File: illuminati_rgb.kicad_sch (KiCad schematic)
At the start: 47 parts, among them IC1 TPS564247DRLR, IC2 SPH0645LM4H-1-8, J1 Conn_02x03_Odd_Even, J2 Conn_01x04, J3 Conn_01x02, J6 Conn_01x02, J7 Conn_01x04, J8 Conn_01x04, Q1 C351406, Q2 C351406, Q3 C351406, Q4 C351406, Q5 C351406, Q6 C351406, Q7 C351406, Q8 C351406, Q9 C351406, SW1 SW_SPST, U1 ESP32-WROOM-32

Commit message: v2 board
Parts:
- removed C5: 22u, Capacitor_SMD:C_0805_2012Metric, symbol Device:C
- removed IC1: TPS564247DRLR, SamacSys_Parts:SOT50P160X60-6N, symbol SamacSys_Parts:TPS564247DRLR
- removed IC2: SPH0645LM4H-1-8, SamacSys_Parts:SPH0645LM4H18, symbol SamacSys_Parts:SPH0645LM4H-1-8
- removed J2, J7, J8: Conn_01x04, TerminalBlock_Phoenix:TerminalBlock_Phoenix_MKDS-1,5-4_1x04_P5.00mm_Horizontal, symbol Connector_Generic:Conn_01x04
- removed J3, J6: Conn_01x02, TerminalBlock_Phoenix:TerminalBlock_Phoenix_MKDS-1,5-2_1x02_P5.00mm_Horizontal, symbol Connector_Generic:Conn_01x02
- removed Q1, Q2, Q3, Q4, Q5, Q6, Q7, Q8, Q9: C351406, Package_TO_SOT_SMD:SOT-23, symbol Device:Q_NMOS_GSD
- removed R10, R6, R9: 10k, Resistor_SMD:R_0805_2012Metric, symbol Device:R
- removed R11: 100k, Resistor_SMD:R_0603_1608Metric_Pad0.98x0.95mm_HandSolder, symbol Device:R
- removed R12: 22k, Resistor_SMD:R_0603_1608Metric_Pad0.98x0.95mm_HandSolder, symbol Device:R
- removed R13: NC, Resistor_SMD:R_0805_2012Metric, symbol Device:R
- removed R14: 0R, Resistor_SMD:R_0805_2012Metric, symbol Device:R
- removed R15: 10k, Resistor_SMD:R_0402_1005Metric, symbol Device:R
- removed R16: 20k, Resistor_SMD:R_0402_1005Metric, symbol Device:R
- removed SW1: SW_SPST, Button_Switch_THT:SW_PUSH_6mm_H5mm, symbol Switch:SW_SPST
- removed U1: ESP32-WROOM-32, RF_Module:ESP32-WROOM-32, symbol RF_Module:ESP32-WROOM-32
- added C1: 10u/1206, Capacitor_SMD:C_1206_3216Metric, symbol Device:C
- added C11, C12, C13, C8: 22u, Capacitor_SMD:C_0805_2012Metric, symbol Device:C
- added D1: B340A, Diode_SMD:D_SMA, symbol Device:D_Schottky
- added IC1: ESP32-C3-WROOM-02-N4, SamacSys_Parts:ESP32C3WROOM02N4, symbol SamacSys_Parts:ESP32-C3-WROOM-02-N4
- added J1: Conn_01x04, TerminalBlock_Phoenix:TerminalBlock_Phoenix_MKDS-1,5-4_1x04_P5.00mm_Horizontal, symbol Connector_Generic:Conn_01x04
- added JP1, JP2, JP3, JP4, JP5: Jumper_2_Bridged, Jumper:SolderJumper-2_P1.3mm_Bridged_RoundedPad1.0x1.5mm, symbol Jumper:Jumper_2_Bridged
- added PS1: AP5100WG-7, SamacSys_Parts:SOT95P285X140-6N, symbol SamacSys_Parts:AP5100WG-7
- added R1: 10k, Resistor_SMD:R_0603_1608Metric, symbol Device:R
- added U1: AMS1117-3.3, Package_TO_SOT_SMD:SOT-223-3_TabPin2, symbol Regulator_Linear:AMS1117-3.3
- added U2, U3, U4: 74HC14, Package_SO:SOIC-14_3.9x8.7mm_P1.27mm, symbol 74xx:74HC14
- C10: renamed from C8; value 10u -> 22u; footprint Capacitor_SMD:C_0805_2012Metric_Pad1.18x1.45mm_HandSolder -> Capacitor_SMD:C_0805_2012Metric
- C2: value 22u -> 10u/1206; footprint Capacitor_SMD:C_0805_2012Metric -> Capacitor_SMD:C_1206_3216Metric
- C3: value 100n -> 22n; footprint Capacitor_SMD:C_0603_1608Metric_Pad1.08x0.95mm_HandSolder -> Capacitor_SMD:C_0603_1608Metric
- C4, C9: value 100n -> 22u; footprint Capacitor_SMD:C_0603_1608Metric_Pad1.08x0.95mm_HandSolder -> Capacitor_SMD:C_0805_2012Metric
- C5: renamed from C1; footprint Capacitor_SMD:C_0805_2012Metric_Pad1.18x1.45mm_HandSolder -> Capacitor_SMD:C_0603_1608Metric
- C7: value 56p -> 100p; footprint Capacitor_SMD:C_0603_1608Metric_Pad1.08x0.95mm_HandSolder -> Capacitor_SMD:C_0603_1608Metric
- L1: value 1.5u -> 10u/C2921170; footprint Inductor_SMD:L_Wuerth_MAPI-4020 -> Inductor_SMD:L_Chilisin_BMRA00040420
- R2, R3, R4, R7: footprint Resistor_SMD:R_0805_2012Metric -> Resistor_SMD:R_0603_1608Metric
- R5, R8: value 10k -> 2k; footprint Resistor_SMD:R_0805_2012Metric -> Resistor_SMD:R_0603_1608Metric
- R6: renamed from R1; footprint Resistor_SMD:R_0805_2012Metric -> Resistor_SMD:R_0603_1608Metric
- renumbered J1 to J2
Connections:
- net +3V3: now also C9.1, R2.1, R3.1, IC1.1 (3V3), R1.1, U1.2 (VO); no longer C4.1, C6.1, C7.1, C9.2, L1.1
- net B1: now also IC1.5 (IO6), U2.5; no longer R8.1
- net B2: now also JP3.2 (B), U2.13
- net B3: now also IC1.13 (IO18), U3.1
- net G1: now also IC1.4 (IO5), U2.3; no longer R5.1
- net G2: now also JP5.2 (B), U2.11
- net G3: now also IC1.14 (IO19), U3.3; no longer R7.1
- net GND: now also C9.2, R5.1, C1.2, C11.2, C12.2, C13.2, C8.2, D1.2 (A), IC1.19 (GND_2), IC1.20 (GND_3), IC1.21 (GND_4), IC1.22 (GND_5), IC1.23 (GND_6), IC1.24 (GND_7), IC1.25 (GND_8), IC1.26 (GND_9), IC1.27 (GND_10), IC1.9 (GND_1), J1.3 (Pin_3), J1.4 (Pin_4), PS1.2 (GND), U1.1 (GND), U2.7 (GND), U3.7 (GND), U4.7 (GND); no longer C3.2, C9.1, R2.2, R3.2, R4.2, R5.2, R7.2
- net R1: now also IC1.3 (IO4), U2.1; no longer R2.1
- net R2: now also IC1.6 (IO7), U2.9; no longer R3.1
- net R3: now also IC1.15 (IO3), U3.5; no longer R4.1
- net VCC: now also R4.2, C1.1, J1.1 (Pin_1), J1.2 (Pin_2), PS1.5 (IN); no longer C3.1
- net boot: now also R3.2, IC1.8 (IO9), JP3.1 (A)
- net esp_en: now also IC1.2 (EN)
- net rx: now also IC1.11 (RXD), JP1.1 (A)
- net tx: now also IC1.12 (TXD), JP2.1 (A)
- net +5V: now reaches L1.2
- net +5V: now also C4.1, C6.1, C7.1, R7.1, C11.1, C12.1, C13.1, C8.1, U1.3 (VI), U2.14 (VCC), U3.14 (VCC), U4.14 (VCC)
- net V_FB: now reaches C7.2
- net V_FB: now also R7.2, R8.1, PS1.3 (FB)
- new net: C3.2, D1.1 (K), L1.1, PS1.6 (SW)
- new net: PS1.4 (EN), R4.1, R5.2
- new net: C3.1, PS1.1 (BST)
- new net B4: IC1.10 (IO10), U3.13
- new net B5: IC1.18 (IO0), U4.5
- new net G4: JP1.2 (B), U3.11
- new net G5: IC1.17 (IO1), U4.3
- new net R4: JP2.2 (B), U3.9
- new net R5: JP4.2 (B), U4.1
- new net RGB Channel1/B: U2.6
- new net RGB Channel1/G: U2.4
- new net RGB Channel1/R: U2.2
- new net RGB Channel2/B: U2.12
- new net RGB Channel2/G: U2.10
- new net RGB Channel2/R: U2.8
- new net RGB Channel3/B: U3.2
- new net RGB Channel3/G: U3.4
- new net RGB Channel3/R: U3.6
- new net RGB Channel4/B: U3.12
- new net RGB Channel4/G: U3.10
- new net RGB Channel4/R: U3.8
- new net RGB Channel5/B: U4.6
- new net RGB Channel5/G: U4.4
- new net RGB Channel5/R: U4.2
- new net gpio2: IC1.16 (IO2), JP4.1 (A), R2.2
- new net gpio8: IC1.7 (IO8), JP5.1 (A), R1.2
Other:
- added sheet RGB Channel1 (rgb.kicad_sch)
- added sheet RGB Channel2 (rgb.kicad_sch)
- added sheet RGB Channel3 (rgb.kicad_sch)
- added sheet RGB Channel4 (rgb.kicad_sch)
- added sheet RGB Channel5 (rgb.kicad_sch)
- note added: "R19 = (10k * 0.81) / (Vo - 0.81)"
- moved on the sheet: C10, C5, H1, H2, J2, R6

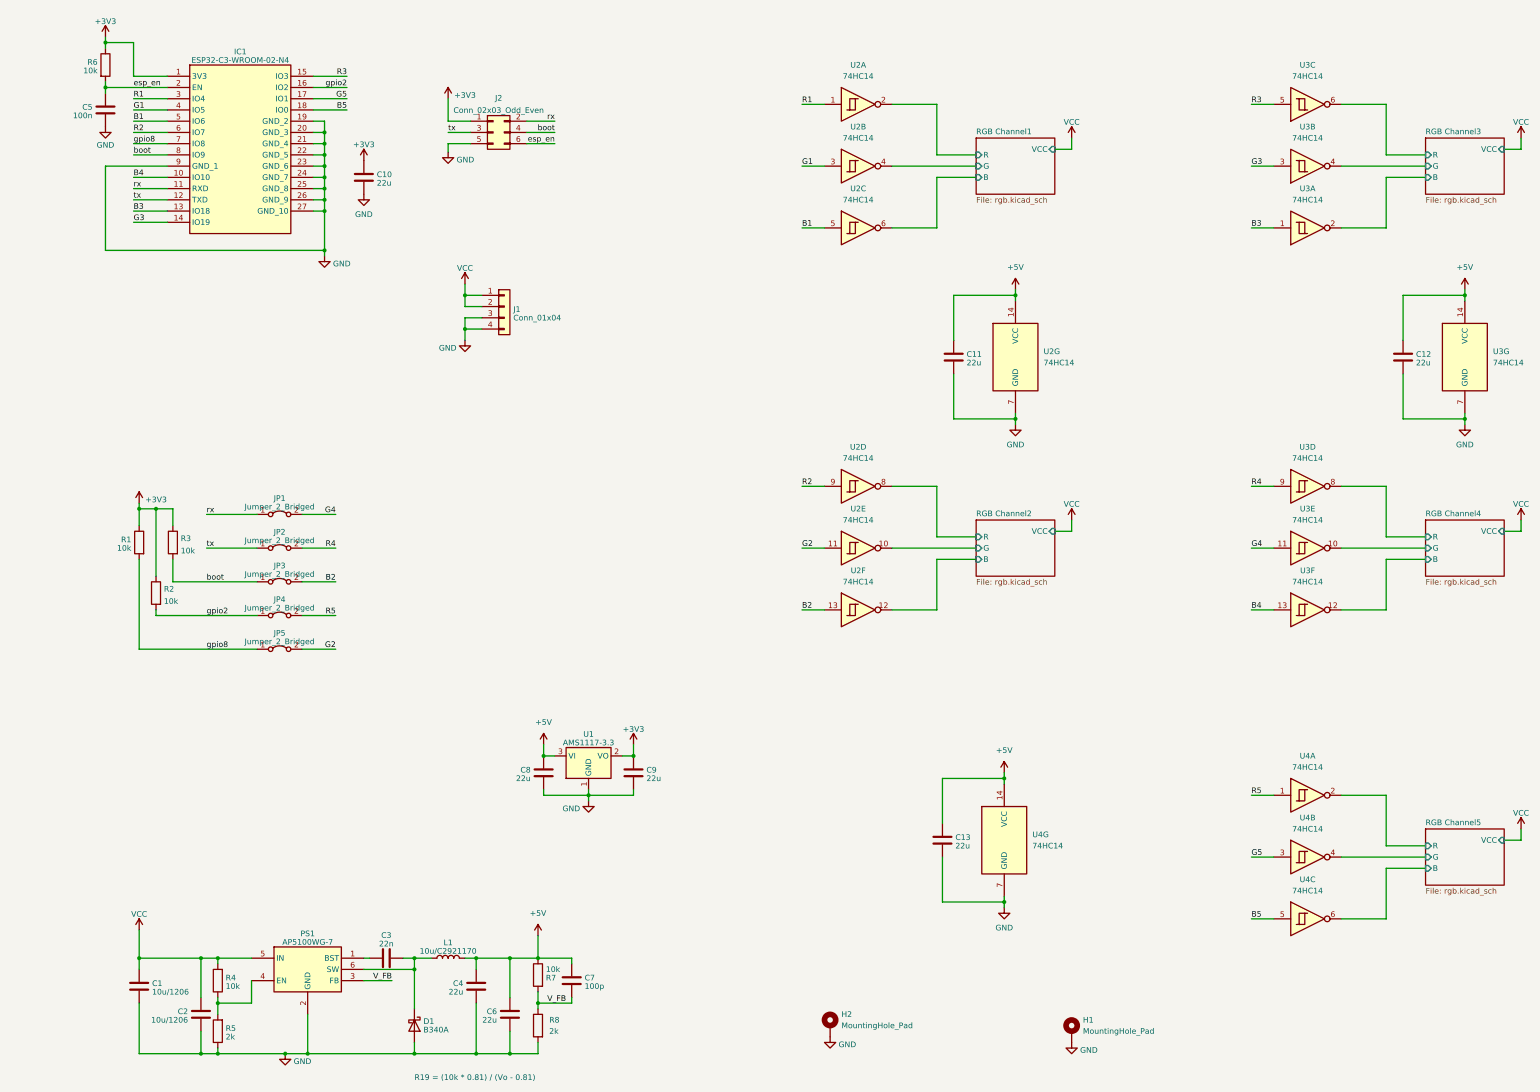
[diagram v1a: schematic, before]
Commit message: V2.1 swap esp32c3 for esp32 and change form factor
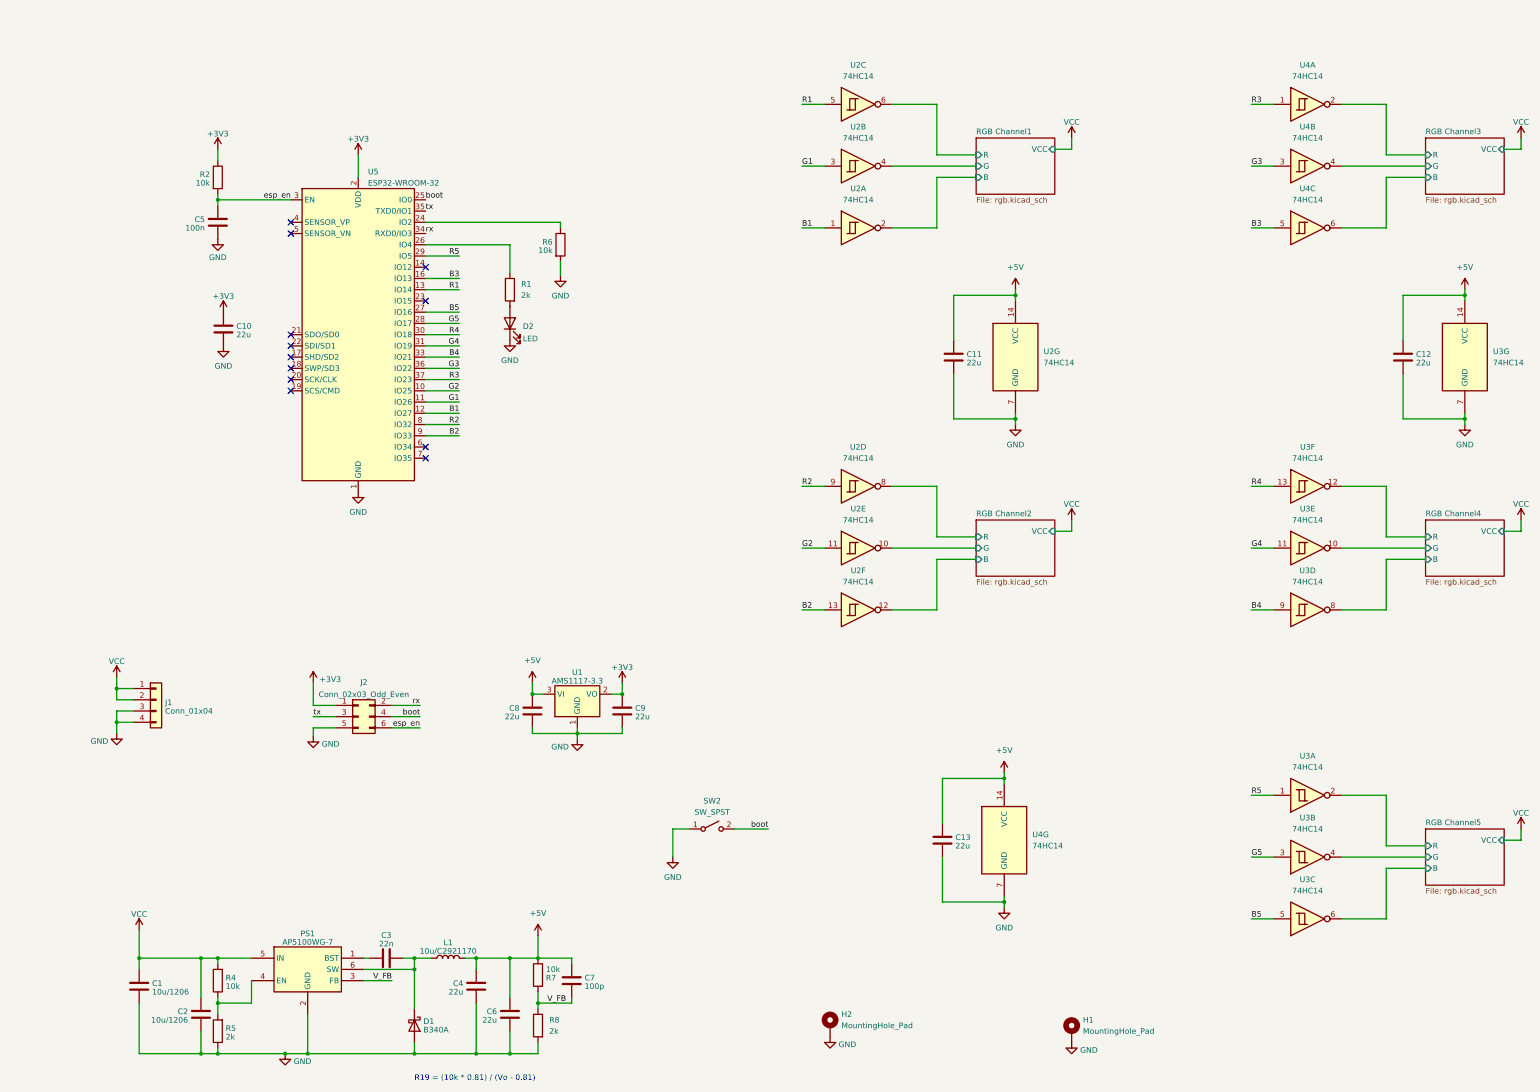
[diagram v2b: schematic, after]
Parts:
- removed IC1: ESP32-C3-WROOM-02-N4, SamacSys_Parts:ESP32C3WROOM02N4, symbol SamacSys_Parts:ESP32-C3-WROOM-02-N4
- removed JP1, JP2, JP3, JP4, JP5: Jumper_2_Bridged, Jumper:SolderJumper-2_P1.3mm_Bridged_RoundedPad1.0x1.5mm, symbol Jumper:Jumper_2_Bridged
- removed R3: 10k, Resistor_SMD:R_0603_1608Metric, symbol Device:R
- added D2: LED, LED_SMD:LED_0805_2012Metric, symbol Device:LED
- added SW2: SW_SPST, Button_Switch_THT:SW_PUSH_6mm_H8mm, symbol Switch:SW_SPST
- added U5: ESP32-WROOM-32, RF_Module:ESP32-WROOM-32, symbol RF_Module:ESP32-WROOM-32
- C1, C2: MPN (none) -> C13585
- C10, C11, C12, C13, C4, C6, C8, C9: MPN (none) -> C45783
- C3: MPN (none) -> C21122
- C5: MPN (none) -> C14663
- C7: MPN (none) -> C1790
- D1: MPN (none) -> C3018525
- J1: MPN (none) -> C192769
- L1: MPN (none) -> C2921170
- PS1: MPN (none) -> C114647
- R1: value 10k -> 2k; MPN (none) -> C22975
- R2, R4, R6, R7: MPN (none) -> C25804
- R5, R8: MPN (none) -> C22975
- U1: MPN (none) -> C6186
- U2, U3, U4: MPN (none) -> C5605
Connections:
- net gpio2 is gone; now on net esp_en: R2.2
- net +3V3: now also U5.2 (VDD); no longer R1.1, R6.1
- net B1: now also U2.1, U5.12 (IO27); no longer U2.5
- net B2: now also U5.9 (IO33)
- net B3: now also U4.5, U5.16 (IO13); no longer U3.1
- net B4: now also U3.9, U5.33 (IO21); no longer U3.13
- net B5: now also U3.5, U5.27 (IO16); no longer U4.5
- net G1: now also U5.11 (IO26)
- net G2: now also U5.10 (IO25)
- net G3: now also U4.3, U5.36 (IO22); no longer U3.3
- net G4: now also U5.31 (IO19)
- net G5: now also U3.3, U5.28 (IO17); no longer U4.3
- net GND: now also R6.2, D2.1 (K), SW2.1 (A), U5.1 (GND), U5.15 (GND), U5.38 (GND), U5.39 (GND)
- net R1: now also U2.5, U5.13 (IO14); no longer U2.1
- net R2: now also U5.8 (IO32)
- net R3: now also U4.1, U5.37 (IO23); no longer U3.5
- net R4: now also U3.13, U5.30 (IO18); no longer U3.9
- net R5: now also U3.1, U5.29 (IO5); no longer U4.1
- net RGB Channel1/B: now also U2.2; no longer U2.6
- net RGB Channel1/R: now also U2.6; no longer U2.2
- net RGB Channel3/B: now also U4.6; no longer U3.2
- net RGB Channel3/G: now also U4.4; no longer U3.4
- net RGB Channel3/R: now also U4.2; no longer U3.6
- net RGB Channel4/B: now also U3.8; no longer U3.12
- net RGB Channel4/R: now also U3.12; no longer U3.8
- net RGB Channel5/B: now also U3.6; no longer U4.6
- net RGB Channel5/G: now also U3.4; no longer U4.4
- net RGB Channel5/R: now also U3.2; no longer U4.2
- net boot: now also SW2.2 (B), U5.25 (IO0)
- net esp_en: now also U5.3 (EN); no longer R6.2
- net rx: now also U5.34 (RXD0/IO3)
- net tx: now also U5.35 (TXD0/IO1)
- net gpio8: no longer names the net of R1.2
- net gpio8: now also D2.2 (A)
- new net: R1.1, U5.26 (IO4)
- new net: R6.1, U5.24 (IO2)
- no-connect marks 0 -> 12
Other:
- moved on the sheet: C10, C8, C9, J1, J2, R6, U1, U2A, U2C, U3A, U3B, U3C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
